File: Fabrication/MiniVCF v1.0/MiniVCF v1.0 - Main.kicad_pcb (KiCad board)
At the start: 2 copper layers, 30 x 82.2 mm, 45 parts, among them J1 JST_BUS, J12 MAIN_BOARD_CONN2, J2 IDC_BUS, J7 CONN_PWR2, J8 MAIN_BOARD_CONN, U1 TL074, U2 TL074

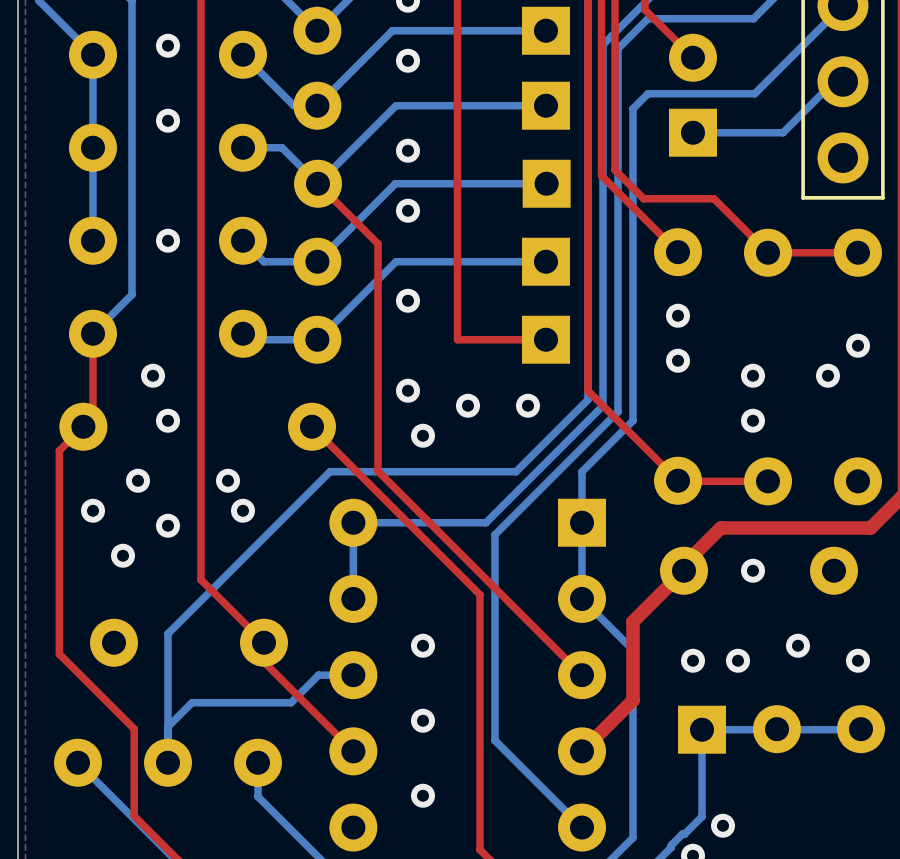
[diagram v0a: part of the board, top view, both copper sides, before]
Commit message: Added a lock hole on control and main board
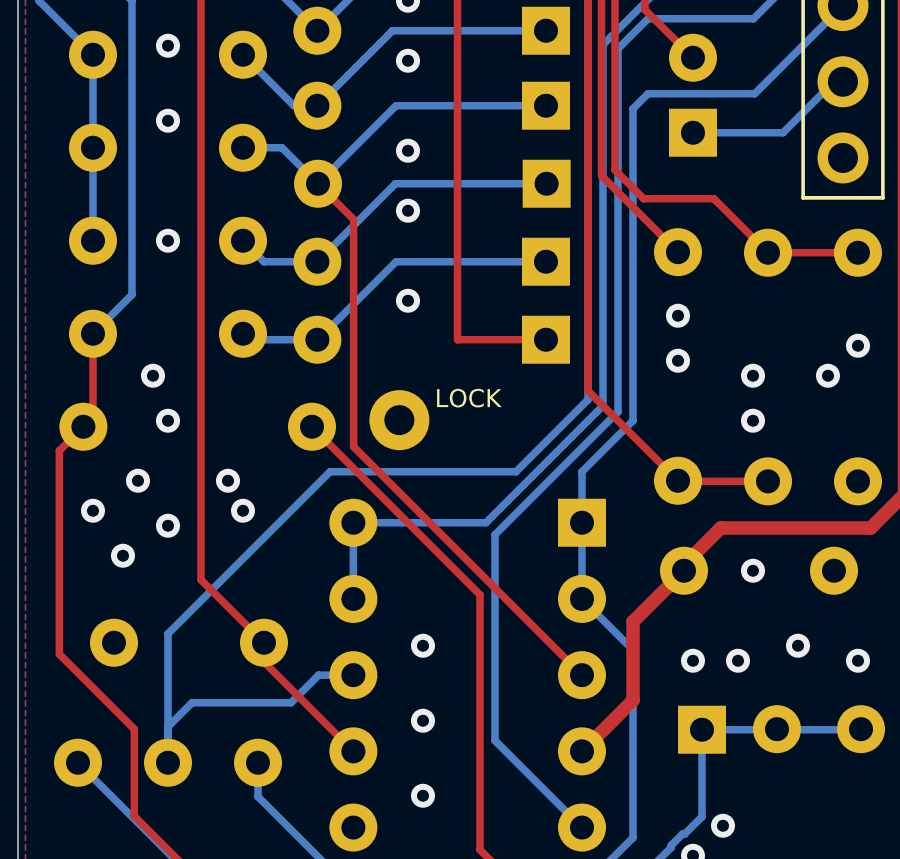
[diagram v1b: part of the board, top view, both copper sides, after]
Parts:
- added REF**: Wire_1mm, benjiaomodular:Wire_1mm, F.Cu at (116.7, 113.0)
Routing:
- net GND2: vias 91 -> 87
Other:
- board text added: "LOCK"
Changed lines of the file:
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@@
   (general
     (thickness 1.6)
-    (drawings 7)
-    (tracks 323)
+    (drawings 10)
+    (tracks 319)
     (zones 0)
-    (modules 45)
+    (modules 46)
     (nets 33)
   )
@@
     (add_net "Net-(R5-Pad2)")
     (add_net RESO_FEEDBACK)
+  )
+  (module benjiaomodular:Wire_1mm (layer F.Cu)
+    (at 116.713 113.03)
+    (fp_text reference REF** (at 0 -2) (layer F.SilkS) hide
+      (effects (font (size 1 1) (thickness 0.15)))
+    )
+    (fp_text value Wire_1mm (at 0 1.5) (layer F.Fab)
+      (effects (font (size 1 1) (thickness 0.15)))
+    )
+    (pad 1 thru_hole circle (at 0 -0.05) (size 2 2) (drill 1) (layers *.Cu *.Mask))
   )
   (module Package_DIP:DIP-14_W7.62mm_Socket (layer B.Cu)
@@
       (net 18 B_CLIPPING_LEDS))
   )
+  (gr_text LOCK (at 118.999 112.268) (layer B.SilkS)
+    (effects (font (size 0.6 0.6) (thickness 0.15)) (justify mirror))
+  )
+  (gr_text LOCK (at 118.999 112.268) (layer F.SilkS)
+    (effects (font (size 0.6 0.6) (thickness 0.15)))
+  )
+  (dimension 12.7 (width 0.15) (layer Dwgs.User)
+    (gr_text "12.700 mm" (at 110.363 116.616) (layer Dwgs.User)
+      (effects (font (size 1 1) (thickness 0.15)))
+    )
+    (feature1 (pts (xy 104.013 113.03) (xy 104.013 115.902421)))
+    (feature2 (pts (xy 116.713 113.03) (xy 116.713 115.902421)))
+    (crossbar (pts (xy 116.713 115.316) (xy 104.013 115.316)))
+    (arrow1a (pts (xy 104.013 115.316) (xy 105.139504 114.729579)))
+    (arrow1b (pts (xy 104.013 115.316) (xy 105.139504 115.902421)))
+    (arrow2a (pts (xy 116.713 115.316) (xy 115.586496 114.729579)))
+    (arrow2b (pts (xy 116.713 115.316) (xy 115.586496 115.902421)))
+  )
   (gr_text "MiniVCF v1.0" (at 109 64.8) (layer B.SilkS)
     (effects (font (size 1 1) (thickness 0.15)) (justify mirror))
@@
   (segment (start 116.6 102.5) (end 114 105.1) (width 0.25) (layer B.Cu) (net 7) (status 20))
   (segment (start 121.6 102.5) (end 116.6 102.5) (width 0.25) (layer B.Cu) (net 7) (status 10))
-  (segment (start 116 107.1) (end 114 105.1) (width 0.25) (layer F.Cu) (net 7) (status 20))
-  (segment (start 122.8 121.48) (end 116 114.68) (width 0.25) (layer F.Cu) (net 7) (status 10))
-  (segment (start 116 114.68) (end 116 107.1) (width 0.25) (layer F.Cu) (net 7))
+  (segment (start 115.189 106.289) (end 114 105.1) (width 0.25) (layer F.Cu) (net 7))
+  (segment (start 122.8 121.48) (end 115.189 113.869) (width 0.25) (layer F.Cu) (net 7))
+  (segment (start 115.189 113.869) (end 115.189 106.289) (width 0.25) (layer F.Cu) (net 7))
   (segment (start 112.2 107.7) (end 111.5 107) (width 0.25) (layer B.Cu) (net 8) (status 20))
   (segment (start 113.98 107.7) (end 112.2 107.7) (width 0.25) (layer B.Cu) (net 8) (status 10))
@@
   (via (at 117 96) (size 0.8) (drill 0.4) (layers F.Cu B.Cu) (net 12))
   (via (at 117 109) (size 0.8) (drill 0.4) (layers F.Cu B.Cu) (net 12))
-  (via (at 117 112) (size 0.8) (drill 0.4) (layers F.Cu B.Cu) (net 12))
-  (via (at 119 112.5) (size 0.8) (drill 0.4) (layers F.Cu B.Cu) (net 12))
-  (via (at 117.5 113.5) (size 0.8) (drill 0.4) (layers F.Cu B.Cu) (net 12))
-  (via (at 121 112.5) (size 0.8) (drill 0.4) (layers F.Cu B.Cu) (net 12))
   (via (at 111 115) (size 0.8) (drill 0.4) (layers F.Cu B.Cu) (net 12))
   (via (at 111.5 116) (size 0.8) (drill 0.4) (layers F.Cu B.Cu) (net 12))
